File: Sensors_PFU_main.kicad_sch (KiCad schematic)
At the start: 1 part, among them U1 AD797

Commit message: deshago el cambio para que pase el check
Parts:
- removed U1: AD797, symbol Amplifier_Operational:AD797
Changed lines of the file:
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@@
-		)
-	)
-	(symbol
-		(lib_id "Amplifier_Operational:AD797")
-		(at 138.43 125.73 0)
-		(unit 1)
-		(exclude_from_sim no)
-		(in_bom yes)
-		(on_board yes)
-		(dnp no)
-		(fields_autoplaced yes)
-		(property "Reference" "U1"
-			(at 148.59 119.3098 0)
-			(effects
-				(font
-					(size 1.27 1.27)
-				)
-			)
-		)
-		(property "Value" "AD797"
-			(at 148.59 121.8498 0)
-			(effects
-				(font
-					(size 1.27 1.27)
-				)
-			)
-		)
-		(property "Footprint" ""
-			(at 139.7 124.46 0)
-			(effects
-				(font
-					(size 1.27 1.27)
-				)
-				(hide yes)
-			)
-		)
-		(property "Datasheet" "https://www.analog.com/media/en/technical-documentation/data-sheets/AD797.pdf"
-			(at 139.7 121.92 0)
-			(effects
-				(font
-					(size 1.27 1.27)
-				)
-				(hide yes)
-			)
-		)
-		(property "Description" "Ultralow Distortion, Ultralow Noise Op Amp, DIP-8/SOIC-8"
-			(at 138.43 125.73 0)
-			(effects
-				(font
-					(size 1.27 1.27)
-				)
-				(hide yes)
-			)
-		)
-		(pin "6"
-		)
-		(pin "1"
-		)
-		(pin "7"
-		)
-		(pin "3"
-		)
-		(pin "4"
-		)
-		(pin "5"
-		)
-		(pin "2"
-		)
-		(pin "8"
-		)
-		(instances
-			(project ""
-				(path "/edac787c-3759-490a-b0c1-b3921b68d461"
-					(reference "U1")
-					(unit 1)
-				)
-			)
 		)
 	)

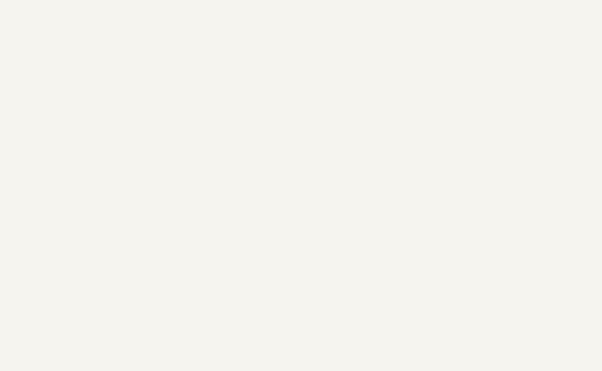
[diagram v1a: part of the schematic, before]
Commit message: Revert "deshago el cambio para que pase el check"
This reverts commit 9426582254d850f4d0d504d2cff88056078614e8.
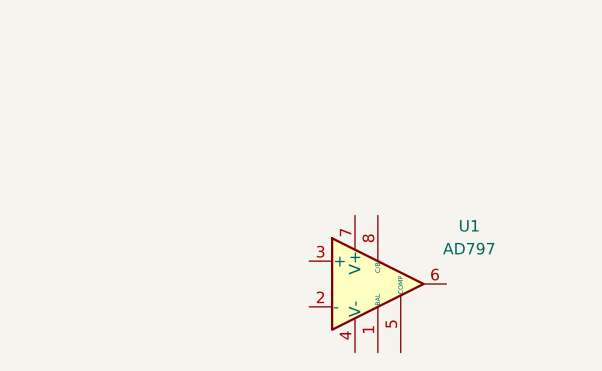
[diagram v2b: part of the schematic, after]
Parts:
- added U1: AD797, symbol Amplifier_Operational:AD797
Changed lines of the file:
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@@
+		)
+	)
+	(symbol
+		(lib_id "Amplifier_Operational:AD797")
+		(at 138.43 125.73 0)
+		(unit 1)
+		(exclude_from_sim no)
+		(in_bom yes)
+		(on_board yes)
+		(dnp no)
+		(fields_autoplaced yes)
+		(property "Reference" "U1"
+			(at 148.59 119.3098 0)
+			(effects
+				(font
+					(size 1.27 1.27)
+				)
+			)
+		)
+		(property "Value" "AD797"
+			(at 148.59 121.8498 0)
+			(effects
+				(font
+					(size 1.27 1.27)
+				)
+			)
+		)
+		(property "Footprint" ""
+			(at 139.7 124.46 0)
+			(effects
+				(font
+					(size 1.27 1.27)
+				)
+				(hide yes)
+			)
+		)
+		(property "Datasheet" "https://www.analog.com/media/en/technical-documentation/data-sheets/AD797.pdf"
+			(at 139.7 121.92 0)
+			(effects
+				(font
+					(size 1.27 1.27)
+				)
+				(hide yes)
+			)
+		)
+		(property "Description" "Ultralow Distortion, Ultralow Noise Op Amp, DIP-8/SOIC-8"
+			(at 138.43 125.73 0)
+			(effects
+				(font
+					(size 1.27 1.27)
+				)
+				(hide yes)
+			)
+		)
+		(pin "6"
+		)
+		(pin "1"
+		)
+		(pin "7"
+		)
+		(pin "3"
+		)
+		(pin "4"
+		)
+		(pin "5"
+		)
+		(pin "2"
+		)
+		(pin "8"
+		)
+		(instances
+			(project ""
+				(path "/edac787c-3759-490a-b0c1-b3921b68d461"
+					(reference "U1")
+					(unit 1)
+				)
+			)
 		)
 	)

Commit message: Revert "modifico otro sch"
This reverts commit 6a0869d378a7460b569b04723fe4b47b4c436e1d.
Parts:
- removed U1: AD797, symbol Amplifier_Operational:AD797
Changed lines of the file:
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@@
 		)
 	)
-	(symbol
-		(lib_id "Amplifier_Operational:AD797")
-		(at 138.43 125.73 0)
-		(unit 1)
-		(exclude_from_sim no)
-		(in_bom yes)
-		(on_board yes)
-		(dnp no)
-		(fields_autoplaced yes)
-		(property "Reference" "U1"
-			(at 148.59 119.3098 0)
-			(effects
-				(font
-					(size 1.27 1.27)
-				)
-			)
-		)
-		(property "Value" "AD797"
-			(at 148.59 121.8498 0)
-			(effects
-				(font
-					(size 1.27 1.27)
-				)
-			)
-		)
-		(property "Footprint" ""
-			(at 139.7 124.46 0)
-			(effects
-				(font
-					(size 1.27 1.27)
-				)
-				(hide yes)
-			)
-		)
-		(property "Datasheet" "https://www.analog.com/media/en/technical-documentation/data-sheets/AD797.pdf"
-			(at 139.7 121.92 0)
-			(effects
-				(font
-					(size 1.27 1.27)
-				)
-				(hide yes)
-			)
-		)
-		(property "Description" "Ultralow Distortion, Ultralow Noise Op Amp, DIP-8/SOIC-8"
-			(at 138.43 125.73 0)
-			(effects
-				(font
-					(size 1.27 1.27)
-				)
-				(hide yes)
-			)
-		)
-		(pin "6"
-		)
-		(pin "1"
-		)
-		(pin "7"
-		)
-		(pin "3"
-		)
-		(pin "4"
-		)
-		(pin "5"
-		)
-		(pin "2"
-		)
-		(pin "8"
-		)
-		(instances
-			(project ""
-				(path "/edac787c-3759-490a-b0c1-b3921b68d461"
-					(reference "U1")
-					(unit 1)
-				)
-			)
-		)
-	)
-	(sheet_instances
-		(path "/"
-			(page "1")
-		)
-	)
-	(embedded_fonts no)
 )

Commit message: modifico otro sch
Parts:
- added U1: AD797, symbol Amplifier_Operational:AD797
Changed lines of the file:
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@@
 		)
 	)
+	(symbol
+		(lib_id "Amplifier_Operational:AD797")
+		(at 138.43 125.73 0)
+		(unit 1)
+		(exclude_from_sim no)
+		(in_bom yes)
+		(on_board yes)
+		(dnp no)
+		(fields_autoplaced yes)
+		(property "Reference" "U1"
+			(at 148.59 119.3098 0)
+			(effects
+				(font
+					(size 1.27 1.27)
+				)
+			)
+		)
+		(property "Value" "AD797"
+			(at 148.59 121.8498 0)
+			(effects
+				(font
+					(size 1.27 1.27)
+				)
+			)
+		)
+		(property "Footprint" ""
+			(at 139.7 124.46 0)
+			(effects
+				(font
+					(size 1.27 1.27)
+				)
+				(hide yes)
+			)
+		)
+		(property "Datasheet" "https://www.analog.com/media/en/technical-documentation/data-sheets/AD797.pdf"
+			(at 139.7 121.92 0)
+			(effects
+				(font
+					(size 1.27 1.27)
+				)
+				(hide yes)
+			)
+		)
+		(property "Description" "Ultralow Distortion, Ultralow Noise Op Amp, DIP-8/SOIC-8"
+			(at 138.43 125.73 0)
+			(effects
+				(font
+					(size 1.27 1.27)
+				)
+				(hide yes)
+			)
+		)
+		(pin "6"
+		)
+		(pin "1"
+		)
+		(pin "7"
+		)
+		(pin "3"
+		)
+		(pin "4"
+		)
+		(pin "5"
+		)
+		(pin "2"
+		)
+		(pin "8"
+		)
+		(instances
+			(project ""
+				(path "/edac787c-3759-490a-b0c1-b3921b68d461"
+					(reference "U1")
+					(unit 1)
+				)
+			)
+		)
+	)
+	(sheet_instances
+		(path "/"
+			(page "1")
+		)
+	)
+	(embedded_fonts no)
 )
